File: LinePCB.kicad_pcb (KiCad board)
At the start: 2 copper layers, 124 parts, among them J1 Conn_02x05_Odd_Even, J2 Conn_01x02, U10 2200, U11 210, U12 Oprocoupler, U13 10k, U14 N channel, U15 D, U16 10K, U4 30k, U5 115k, U6 BSP89, U7 Optocoupler, U8 210, U9 2200

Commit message: Finished Placement
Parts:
- removed H4, H5, H6, H7, H8: MountingHole, MountingHole:MountingHole_3.2mm_M3_DIN965_Pad
- added U1: MCP3008, footprints:SOIC16-N_MC_MCH-L, F.Cu at (100.6, 104.2)
- added U17: Conn_01x02, SMDPads:Pads, B.Cu at (34.9, 99.5)
- added U2: MCP3008, footprints:SOIC16-N_MC_MCH-L, F.Cu at (95.0, 87.5)
- added U3: MCP3008, footprints:SOIC16-N_MC_MCH-L, F.Cu at (107.9, 87.7)
- D1, D10, D11, D12, D13, D14, D15, D16, D17, D18, D19, D2, D20, D21, D22, D23, D24, D25, D26, D27, D28, D29, D3, D30, D31, D32, D33, D34, D35, D36, D37, D38, D39, D4, D40, D41, D42, D43, D44, D45, D46, D47, D48, D49, D5, D6, D7, D8, D9, R1, R10, R11, R12, R13, R14, R15, R16, R17, R18, R19, R2, R20, R21, R22, R23, R24, R25, R26, R27, R28, R29, R3, R30, R31, R32, R33, R34, R35, R36, R37, R38, R39, R4, R40, R41, R42, R43, R44, R45, R46, R47, R48, R5, R6, R7, R8, R9, U11, U13, U16, U4, U5, U8: moved to B.Cu
- moved U7 229.8 mm to (19.7, 94.9), turned to 90 degrees
- moved U12 229.0 mm to (19.8, 113.2), turned to 90 degrees
- moved U14 226.2 mm to (37.7, 78.4), turned to -25 degrees
- moved U6 220.9 mm to (42.4, 119.4), turned to -155 degrees
- moved H1 219.2 mm to (19.0, 100.0)
- moved D49 217.8 mm to (28.0, 94.1), turned to 180 degrees
- moved R52 207.8 mm to (54.5, 97.8), turned to 90 degrees
- moved U8 207.1 mm to (24.1, 99.3), turned to -90 degrees
- moved U11 205.8 mm to (26.6, 109.3), turned to -90 degrees
- moved U4 203.9 mm to (26.5, 86.7), turned to -90 degrees
- moved U13 202.3 mm to (28.0, 97.5)
- moved U5 199.2 mm to (30.8, 85.0), turned to 90 degrees
- moved U16 196.9 mm to (32.3, 78.8), turned to 180 degrees
- moved D25 187.6 mm to (47.6, 96.6), turned to 176.25 degrees
- moved D26 187.6 mm to (47.9, 93.1), turned to 172.5 degrees
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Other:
- board outline added: 168.2 x 110 mm

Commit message: Finished PCB
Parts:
- U1, U2, U3: moved to B.Cu
- moved U4 20.6 mm to (26.3, 107.3)
- moved U12 19.2 mm to (19.8, 94.1)
- moved U11 18.7 mm to (26.4, 90.5)
- moved U7 18.6 mm to (19.7, 113.5)
- moved U8 13.4 mm to (25.7, 112.6)
- moved R52 4.50 mm to (52.3, 93.9), turned to -90 degrees
- moved U1 2.31 mm to (101.5, 106.3)
- moved U2 1.80 mm to (93.4, 86.8), turned to 0 degrees
- moved U3 1.27 mm to (108.9, 86.9), turned to 0 degrees
- moved U5 0.64 mm to (31.4, 85.0), turned to -90 degrees
- turned D17 to -124 degrees
- turned R44 to 34 degrees
- turned D5 to -34 degrees
- turned R8 to -56 degrees
- turned D29 to 146 degrees
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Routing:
- net GND: track 0.00 -> 693.4 mm, vias 0 -> 22
- net 3.3V: track 0.00 -> 585.6 mm, vias 0 -> 24
- net 12V: track 0.00 -> 295.1 mm
- net Kicker: track 0.00 -> 204.8 mm, vias 0 -> 2
- net MOSI: track 0.00 -> 178.0 mm, vias 0 -> 1
- net SCK1: track 0.00 -> 177.5 mm, vias 0 -> 3
- net MISO: track 0.00 -> 161.9 mm, vias 0 -> 2
- net CS1: track 0.00 -> 156.6 mm, vias 0 -> 1
- net CS2: track 0.00 -> 130.4 mm, vias 0 -> 1
- net Ch12: track 0.00 -> 127.4 mm, vias 0 -> 2
- net CS3: track 0.00 -> 118.5 mm, vias 0 -> 1
- net Ch13: track 0.00 -> 116.5 mm, vias 0 -> 2
- net Ch1: track 0.00 -> 111.1 mm, vias 0 -> 2
- net Ch11: track 0.00 -> 105.7 mm, vias 0 -> 2
- net Ch24: track 0.00 -> 104.5 mm, vias 0 -> 3
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- added copper zone on B.Cu, net GND
- added copper zone on F.Cu, net GND
- added copper zone on In1.Cu, net GND
- added copper zone on In2.Cu, net GND
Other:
- outline, holes or cut-outs redrawn
- copper layers 2 -> 4

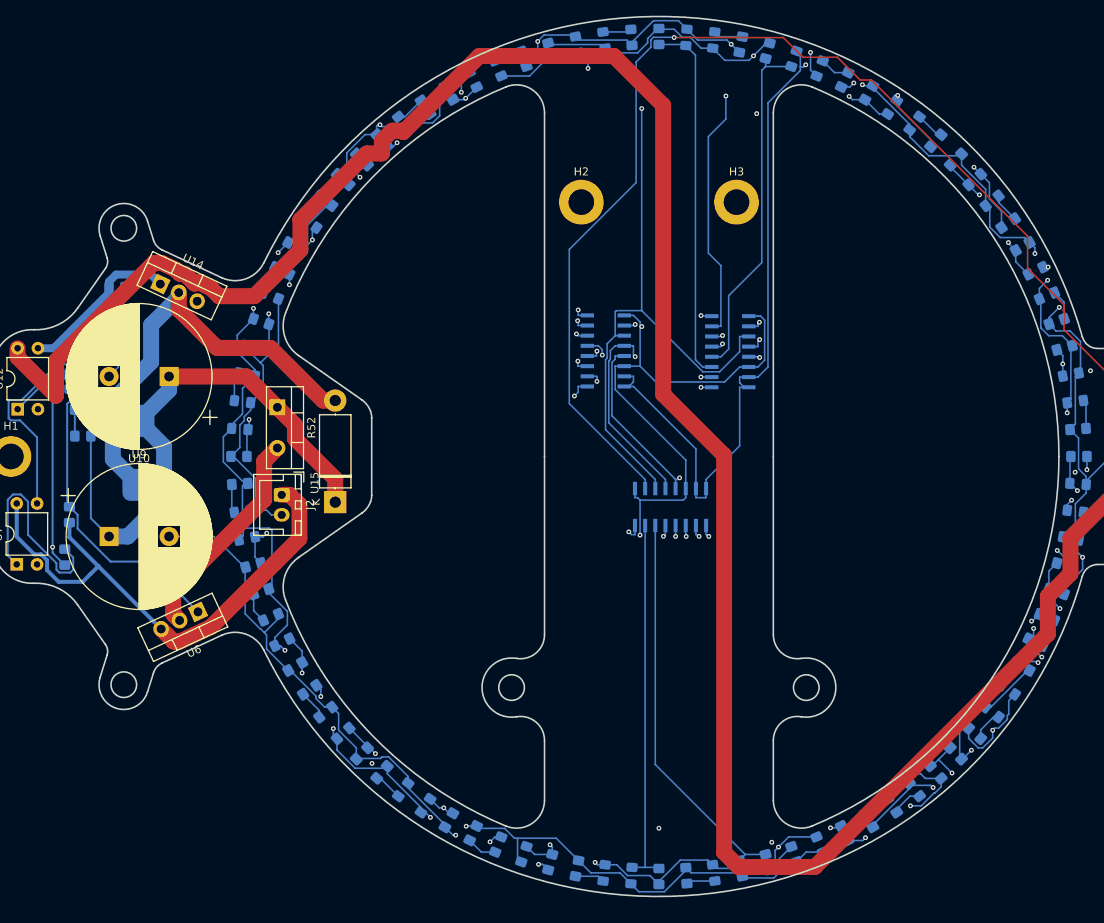
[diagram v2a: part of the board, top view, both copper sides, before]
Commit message: Fixed Main 12V trace
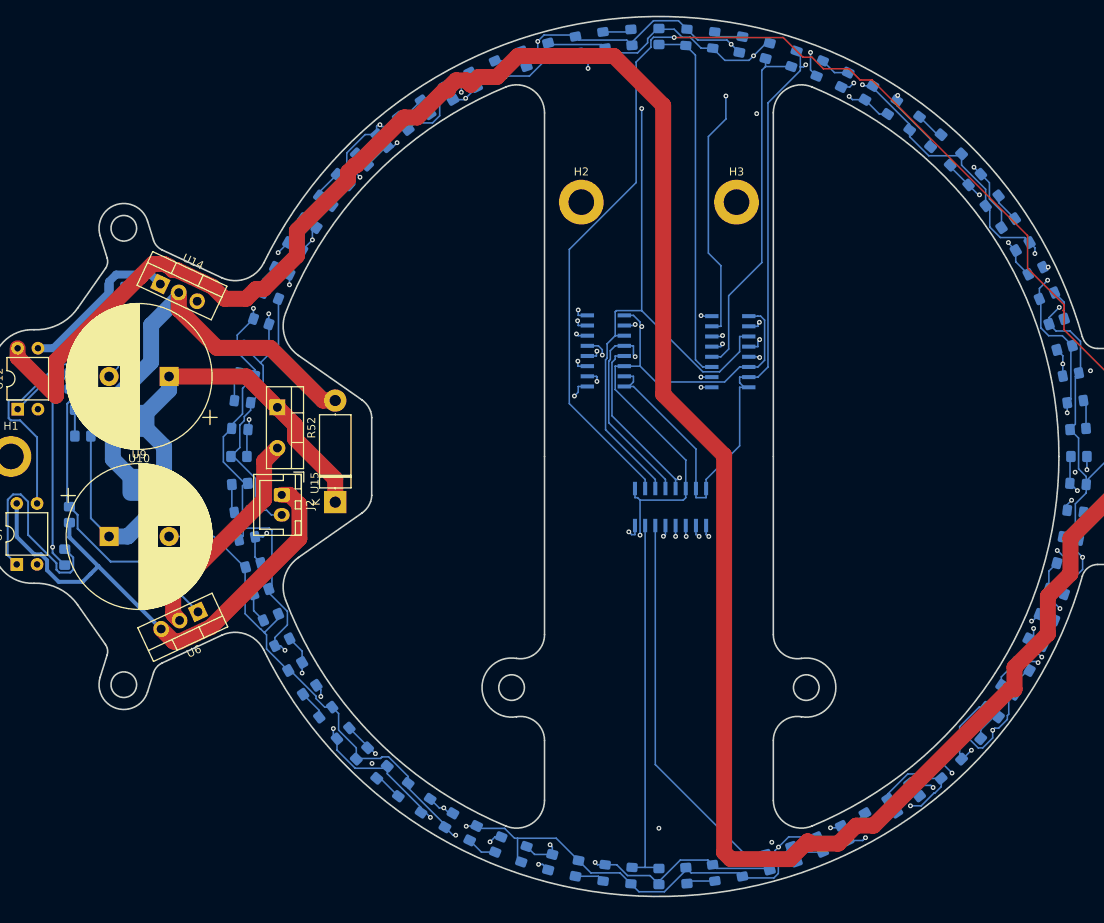
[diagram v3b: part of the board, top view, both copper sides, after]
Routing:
- net 12V: track 295.1 -> 295.8 mm

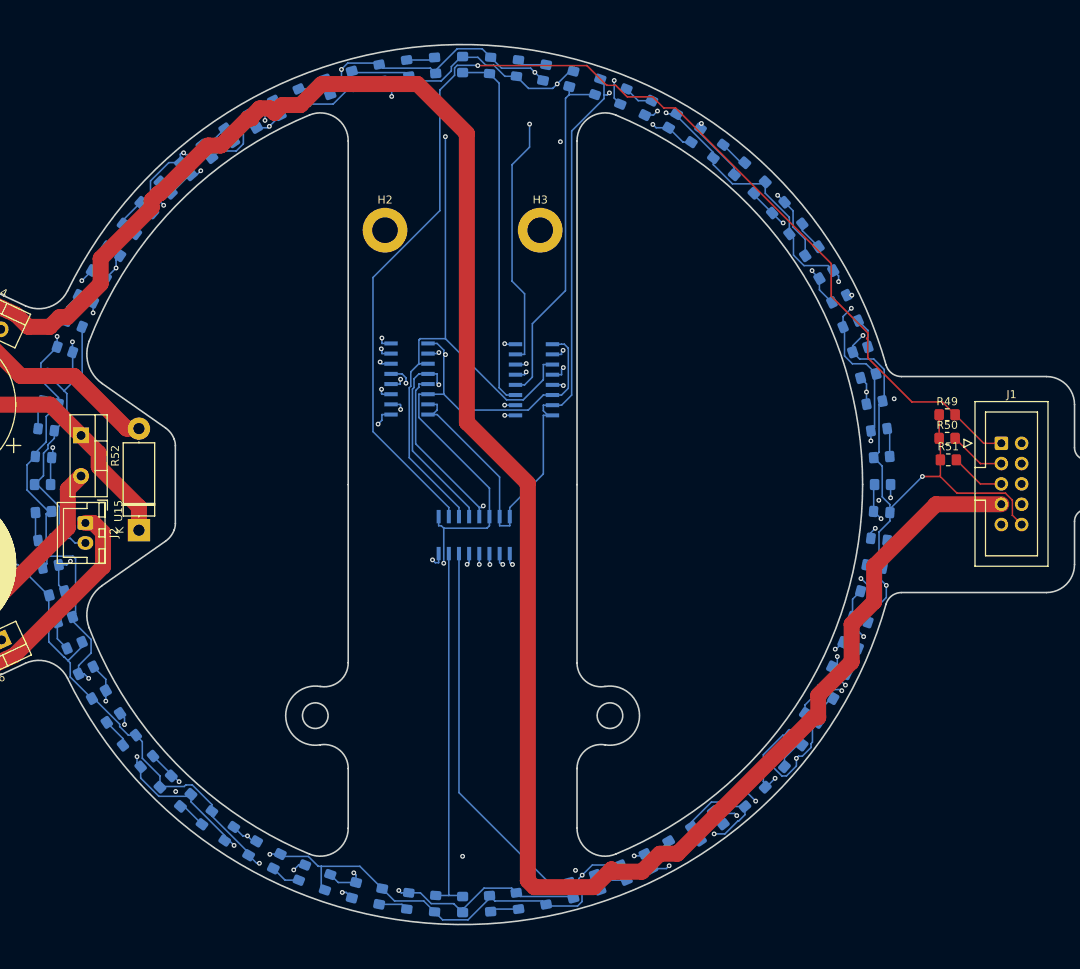
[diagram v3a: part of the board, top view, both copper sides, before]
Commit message: fixed all 120 fucking pcb errors, its 12:30am and i have school tomorrow
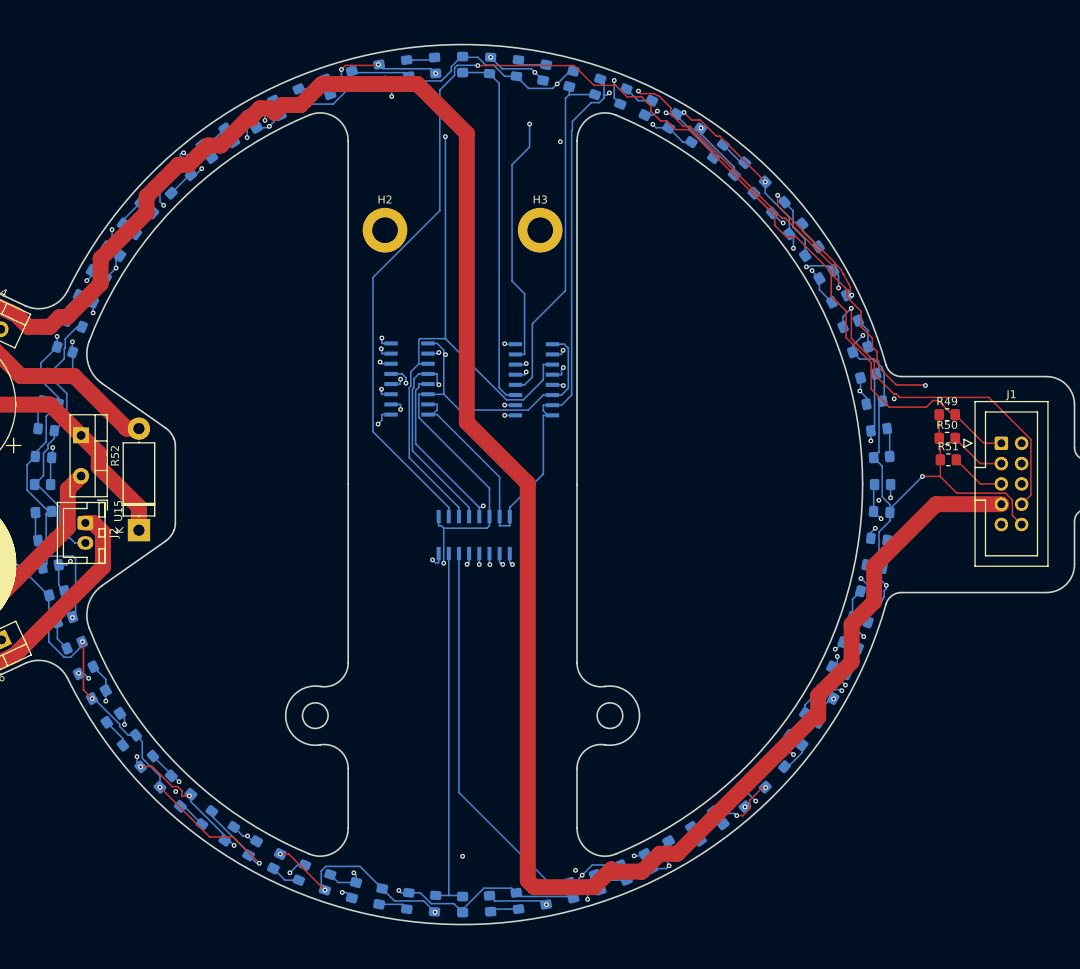
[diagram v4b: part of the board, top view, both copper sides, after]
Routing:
- net GND: track 693.4 -> 752.0 mm, vias 22 -> 31
- net 3.3V: track 585.6 -> 602.5 mm, vias 24 -> 36
- net Kicker: track 204.8 -> 208.7 mm
- net Ch3: track 92.2 -> 95.3 mm
- net CS1: track 156.6 -> 159.7 mm
- net Ch2: track 98.6 -> 101.5 mm
- net Ch1: track 111.1 -> 113.9 mm
- net SCK1: track 177.5 -> 179.9 mm
- net Ch10: track 90.7 -> 92.8 mm
- net Ch11: track 105.7 -> 107.7 mm
- net Ch15: track 79.0 -> 80.8 mm
- net Ch24: track 104.5 -> 106.2 mm
- net MISO: track 161.9 -> 163.6 mm
- net Ch9: track 74.7 -> 76.1 mm
- net MOSI: track 178.0 -> 179.2 mm
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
